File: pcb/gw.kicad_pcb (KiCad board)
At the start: 2 copper layers, 19 parts, among them IC1 ATMEGA8A-P, P1 CONN_CLUNET, P2 USB_OTG, Q1 BC849, U1 FT232RL, Y1 Crystal

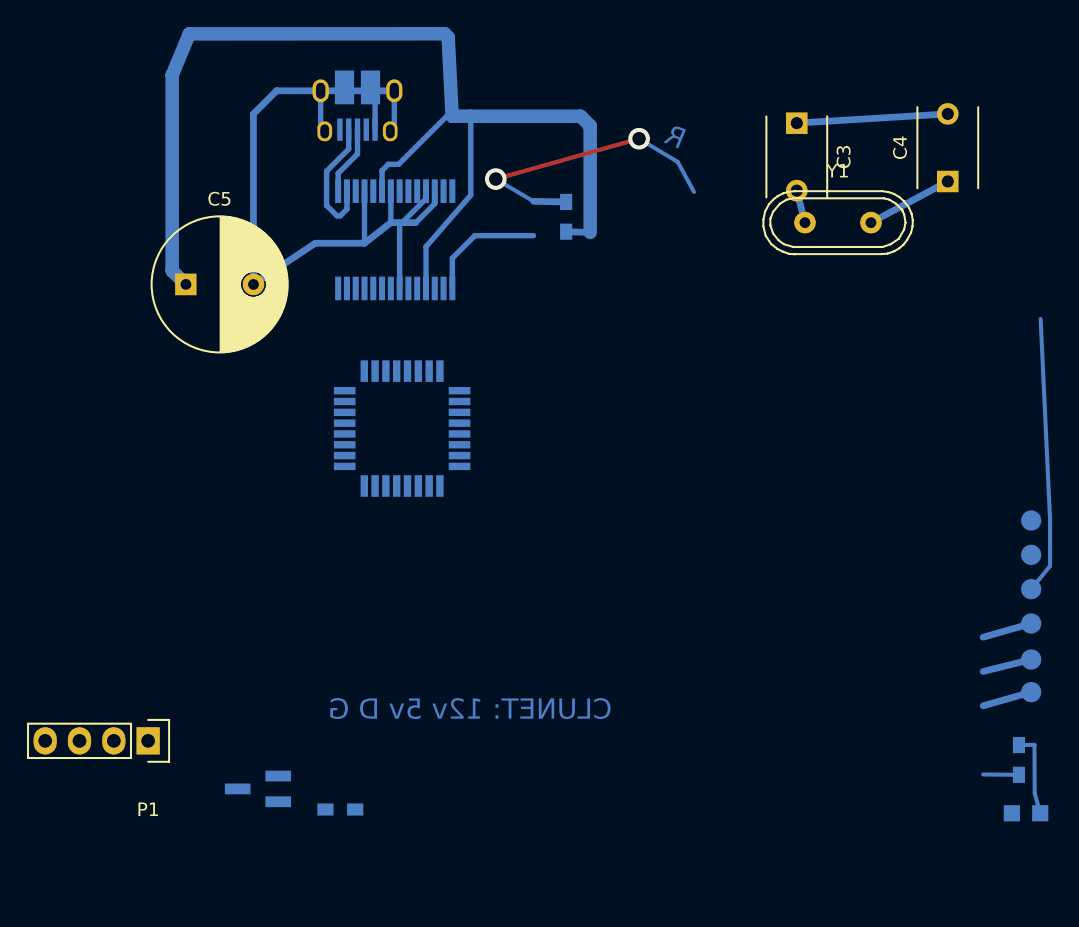
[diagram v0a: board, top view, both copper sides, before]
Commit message: Switch PCB sides, TQFP32 atmega
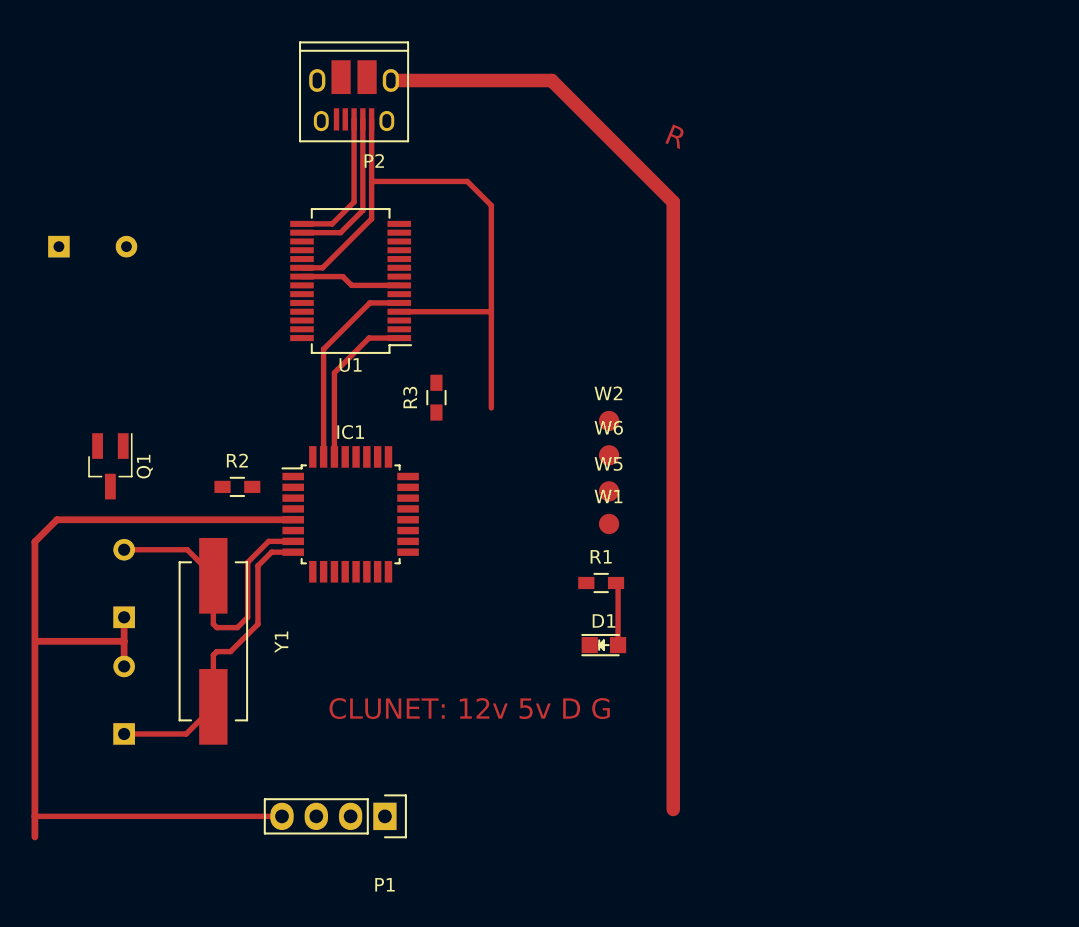
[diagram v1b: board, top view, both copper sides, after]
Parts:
- removed W3: VCC, Measurement_Points:Measurement_Point_Round-SMD-Pad_Small
- removed W4: GND, Measurement_Points:Measurement_Point_Round-SMD-Pad_Small
- C3, C4, C5: moved to B.Cu
- D1, IC1, P2, Q1, R1, R2, R3, U1, W1, W2, W5, W6: moved to F.Cu
- Y1: footprint Crystals:Crystal_HC49-U_Vertical -> Crystals:Crystal_HC49-SD_SMD
- moved C4 73.4 mm to (84.8, 71.6)
- moved C3 61.8 mm to (84.8, 63.0), turned to 90 degrees
- moved Y1 55.7 mm to (91.4, 64.8), turned to 270 degrees
- moved W1 33.6 mm to (120.7, 56.1)
- moved W5 33.6 mm to (120.7, 53.7)
- moved D1 33.6 mm to (120.3, 65.0)
- moved W2 33.6 mm to (120.7, 48.5)
- moved W6 33.6 mm to (120.7, 51.0)
- moved R1 33.6 mm to (120.1, 60.5), turned to 0 degrees
- moved Q1 26.3 mm to (83.8, 51.8), turned to 270 degrees
- moved R2 25.1 mm to (93.2, 53.3)
- moved P1 18.4 mm to (104.1, 77.7)
- moved R3 16.5 mm to (108.0, 46.7), turned to 90 degrees
- moved C5 9.80 mm to (80.0, 35.6)
- moved IC1 7.41 mm to (101.6, 55.4), turned to 0 degrees
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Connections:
- net Net-(IC1-Pad15) renamed MOSI
- net Net-(IC1-Pad16) renamed MISO
- net Net-(IC1-Pad17) renamed SCK
- net Net-(P2-Pad2) renamed /USBD-
- net Net-(P2-Pad3) renamed /USBD+
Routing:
- net GND: track 75.0 -> 146.7 mm
- net /Reset: track 43.1 -> 0.00 mm, vias 2 -> 0
- net VCC: track 86.9 -> 45.4 mm
- net /xtal1: track 2.44 -> 22.0 mm
- net /xtal2: track 6.45 -> 22.9 mm
- net UART_TX: track 0.00 -> 15.0 mm
- net /USBD+: track 5.14 -> 10.6 mm
- net SCK: track 3.70 -> 0.00 mm
- net MOSI: track 3.70 -> 0.00 mm
- net MISO: track 3.67 -> 0.00 mm
- net UART_RX: track 8.94 -> 12.1 mm
- net Net-(IC1-Pad13): track 2.65 -> 0.00 mm
- net /USBD-: track 9.65 -> 11.9 mm
- net Net-(D1-Pad2): track 6.27 -> 4.66 mm
